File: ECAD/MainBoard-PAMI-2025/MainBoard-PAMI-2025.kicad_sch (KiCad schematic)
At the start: 52 parts, among them J1 Selecteur-Robot, J10 Serial, J11 Con_Batt, J12 BAU, J13 OLED, J2 USB_B, J3 Tirette, J4 Servo, J5 Sensor_Right, J6 Sensor_Left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

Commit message: update PCB
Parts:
- removed J12: BAU, Connector_Molex:Molex_KK-396_A-41791-0002_1x02_P3.96mm_Vertical, symbol Connector_Generic:Conn_01x02
- removed J3: Tirette, Connector_Molex:Molex_KK-254_AE-6410-02A_1x02_P2.54mm_Vertical, symbol Connector_Generic:Conn_01x02
- removed J9: Conn_01x08, symbol Connector_Generic:Conn_01x08
- removed U4, U5: TMC2208_SILENTSTEPSTICK, TMC2208_SILENTSTEPSTICK:MODULE_TMC2208_SILENTSTEPSTICK, symbol TMC2208_SILENTSTEPSTICK:TMC2208_SILENTSTEPSTICK
- added H4: MountingHole, MountingHole:MountingHole_3.2mm_M3, symbol Mechanical:MountingHole
- added SW2: SW_Reed, symbol Switch:SW_Reed
- added SW3: SW_SPDT, footprints:SK-12D10 1P2T, symbol Switch:SW_SPDT
- added U3, U4: TMC2208_SILENTSTEPSTICK, PAMI-2025:Step-Stick Driver Bottom Entry Version, symbol PAMI-2025:TMC2208_SILENTSTEPSTICK
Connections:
- net +3.3V: now also U3.10 (VIO), U4.10 (VIO)
- net +5VP: now also SW3.3 (C), U3.16 (VM), U4.16 (VM)
- net +BATT: now also SW3.2 (B)
- net EnDriver: now also U3.1 (EN), U4.1 (EN)
- net GND: now also SW2.1, U3.15 (GND), U3.9 (GND), U4.15 (GND), U4.9 (GND)
- net LeftDir: now also U4.8 (DIR)
- net LeftMS1: now also U3.2 (MS1), U4.2 (MS1)
- net LeftMS2: now also U3.3 (MS2), U4.3 (MS2)
- net LeftStep: now also U4.7 (STEP)
- net RightDir: now also U3.8 (DIR)
- net RightStep: now also U3.7 (STEP)
- net Tirette: now also SW2.2
- net at J7.1 (Pin_1): now also U4.14 (OA2)
- net at J7.2 (Pin_2): now also U4.13 (OA1)
- net at J7.3 (Pin_3): now also U4.12 (OB1)
- net at J7.4 (Pin_4): now also U4.11 (OB2)
- net at J8.1 (Pin_1): now also U3.14 (OA2)
- net at J8.2 (Pin_2): now also U3.13 (OA1)
- net at J8.3 (Pin_3): now also U3.12 (OB1)
- net at J8.4 (Pin_4): now also U3.11 (OB2)
- no-connect marks 22 -> 19
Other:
- moved on the sheet: H1, H2, H3

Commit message: Everything that need to be here :)
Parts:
- removed J5: Sensor_Right, Connector_IDC:IDC-Header_2x03_P2.54mm_Vertical, symbol Connector_Generic:Conn_02x03_Odd_Even
- removed J6: Sensor_Left, Connector_IDC:IDC-Header_2x03_P2.54mm_Vertical, symbol Connector_Generic:Conn_02x03_Odd_Even
- added J3: Sensor_RIGHT, Connector_PinSocket_2.54mm:PinSocket_1x06_P2.54mm_Vertical, symbol Connector_Generic:Conn_01x06
- added J5: Sensor_LEFT, Connector_PinSocket_2.54mm:PinSocket_1x06_P2.54mm_Vertical, symbol Connector_Generic:Conn_01x06
- added J6: Servo, Connector_PinHeader_2.54mm:PinHeader_1x03_P2.54mm_Vertical, symbol Connector_Generic:Conn_01x03
- added R12: 330R, Resistor_SMD:R_1206_3216Metric_Pad1.30x1.75mm_HandSolder, symbol Device:R_Small
- J11: footprint Connector_AMASS:AMASS_XT30U-F_1x02_P5.0mm_Vertical -> PAMI-2025:LP-e6 Batterie
- J13: footprint Connector_Molex:Molex_KK-254_AE-6410-04A_1x04_P2.54mm_Vertical -> Connector_PinSocket_2.54mm:PinSocket_1x04_P2.54mm_Vertical
- SW2: footprint (none) -> Button_Switch_SMD:SW_SPST_REED_CT05-XXXX-G1
- SW3: footprint footprints:SK-12D10 1P2T -> PAMI-2025:UB16SKW03N-C
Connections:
- net +3.3V: now also J3.1 (Pin_1), J5.1 (Pin_1)
- net +5VP: now also SW3.2 (C), J6.2 (Pin_2); no longer SW3.3 (C)
- net +BATT: now also SW3.1 (B); no longer SW3.2 (B)
- net BotNum01: now also J1.3 (Pin_3); no longer J1.4 (Pin_4)
- net BotNum02: now also J1.4 (Pin_4); no longer J1.3 (Pin_3)
- net GND: now also J3.2 (Pin_2), J5.2 (Pin_2), J6.3 (Pin_3)
- net GPIOI_LEFT: now also J5.5 (Pin_5)
- net GPIOI_RIGHT: now also J3.5 (Pin_5)
- net SCL: now also J3.3 (Pin_3), J5.3 (Pin_3)
- net SDA: now also J3.4 (Pin_4), J5.4 (Pin_4)
- net XSHUT_LEFT: now also J5.6 (Pin_6)
- net XSHUT_RIGHT: now also J3.6 (Pin_6)
- net Servo02: now reaches U1.4 (GPIO4/TOUCH4/ADC1_CH3)
- net Servo02: now also R12.1
- net Servo renamed Servo01
- new net: J6.1 (Pin_1), R12.2
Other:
- moved on the sheet: J4, R6

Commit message: Quick routing
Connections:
- net +3.3V: now also C10.2, D1.1 (VDD)
- net +5VP: no longer C10.2, D1.1 (VDD)
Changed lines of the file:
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@@
 	)
 	(symbol
+		(lib_id "power:+3.3V")
+		(at 41.91 46.99 0)
+		(unit 1)
+		(exclude_from_sim no)
+		(in_bom yes)
+		(on_board yes)
+		(dnp no)
+		(fields_autoplaced yes)
+		(property "Reference" "#PWR019"
+			(at 41.91 50.8 0)
+			(effects
+				(font
+					(size 1.27 1.27)
+				)
+				(hide yes)
+			)
+		)
+		(property "Value" "+3.3V"
+			(at 41.91 41.91 0)
+			(effects
+				(font
+					(size 1.27 1.27)
+				)
+			)
+		)
+		(property "Footprint" ""
+			(at 41.91 46.99 0)
+			(effects
+				(font
+					(size 1.27 1.27)
+				)
+				(hide yes)
+			)
+		)
+		(property "Datasheet" ""
+			(at 41.91 46.99 0)
+			(effects
+				(font
+					(size 1.27 1.27)
+				)
+				(hide yes)
+			)
+		)
+		(property "Description" ""
+			(at 41.91 46.99 0)
+			(effects
+				(font
+					(size 1.27 1.27)
+				)
+				(hide yes)
+			)
+		)
+		(pin "1"
+		)
+		(instances
+			(project "MainBoard-PAMI-2025"
+				(path "/d3e1aeb6-1412-4438-ac7d-372534bf2609"
+					(reference "#PWR019")
+					(unit 1)
+				)
+			)
+		)
+	)
+	(symbol
 		(lib_id "power:+5VP")
 		(at 54.61 27.94 0)
@@
 					(unit 1)
 				)
-			)
-		)
-	)
-	(symbol
-		(lib_id "power:+5VP")
-		(at 41.91 46.99 0)
-		(unit 1)
-		(exclude_from_sim no)
-		(in_bom yes)
-		(on_board yes)
-		(dnp no)
-		(fields_autoplaced yes)
-		(property "Reference" "#PWR019"
-			(at 41.91 50.8 0)
-			(effects
-				(font
-					(size 1.27 1.27)
-				)
-				(hide yes)
-			)
-		)
-		(property "Value" "+5VP"
-			(at 41.91 41.91 0)
-			(effects
-				(font
-					(size 1.27 1.27)
-				)
-			)
-		)
-		(property "Footprint" ""
-			(at 41.91 46.99 0)
-			(effects
-				(font
-					(size 1.27 1.27)
-				)
-				(hide yes)
-			)
-		)
-		(property "Datasheet" ""
-			(at 41.91 46.99 0)
-			(effects
-				(font
-					(size 1.27 1.27)
-				)
-				(hide yes)
-			)
-		)
-		(property "Description" ""
-			(at 41.91 46.99 0)
-			(effects
-				(font
-					(size 1.27 1.27)
-				)
-				(hide yes)
-			)
-		)
-		(pin "1"
-		)
-		(instances
-			(project "MainBoard-PAMI-2025"
-				(path "/d3e1aeb6-1412-4438-ac7d-372534bf2609"
-					(reference "#PWR019")
-					(unit 1)
-				)
-			)
-			(project "LidarBoard-2023"
-				(path "/e63e39d7-6ac0-4ffd-8aa3-1841a4541b55"
-					(reference "#PWR0125")
-					(unit 1)
-				)

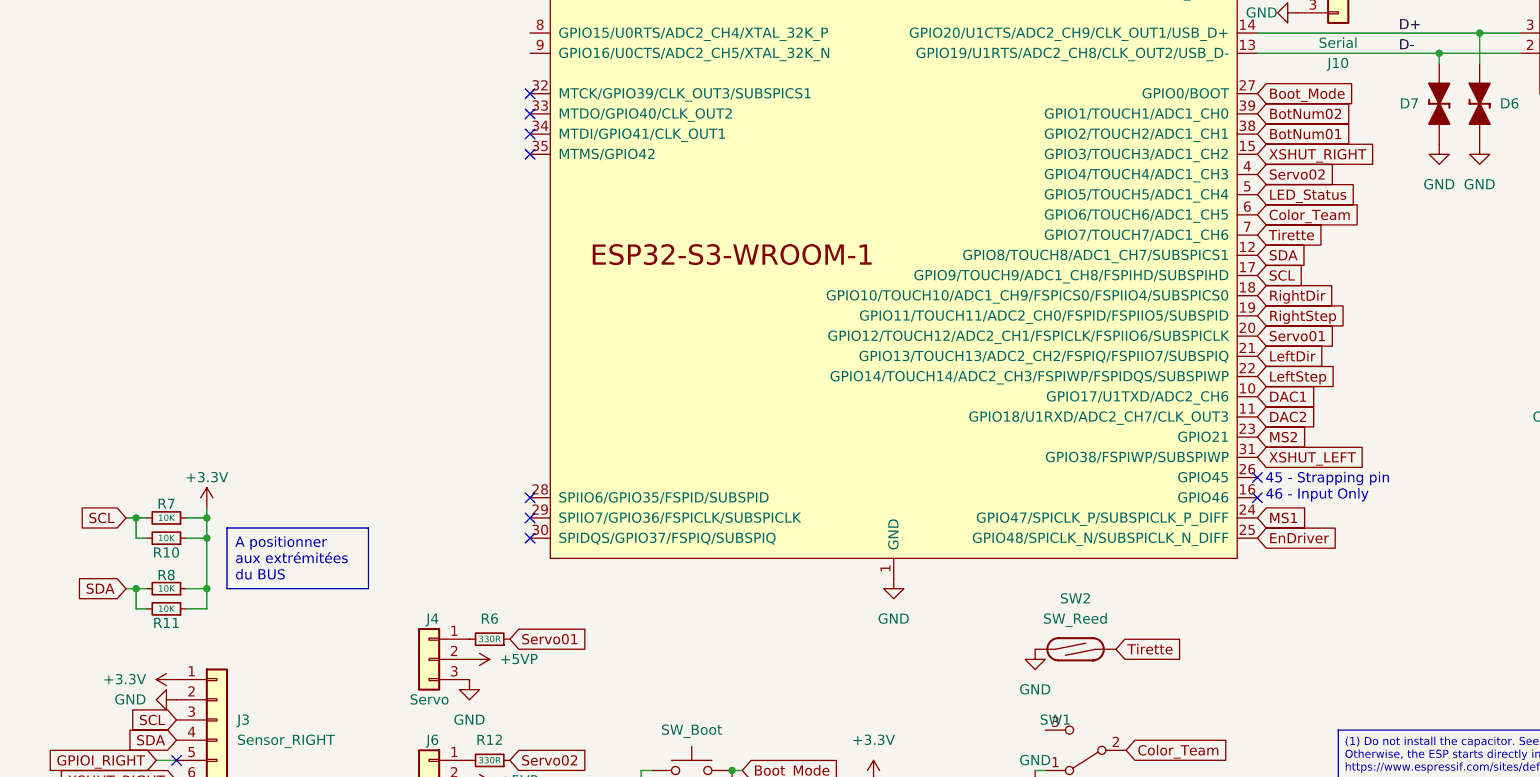
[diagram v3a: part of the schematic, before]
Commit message: Optimize routing
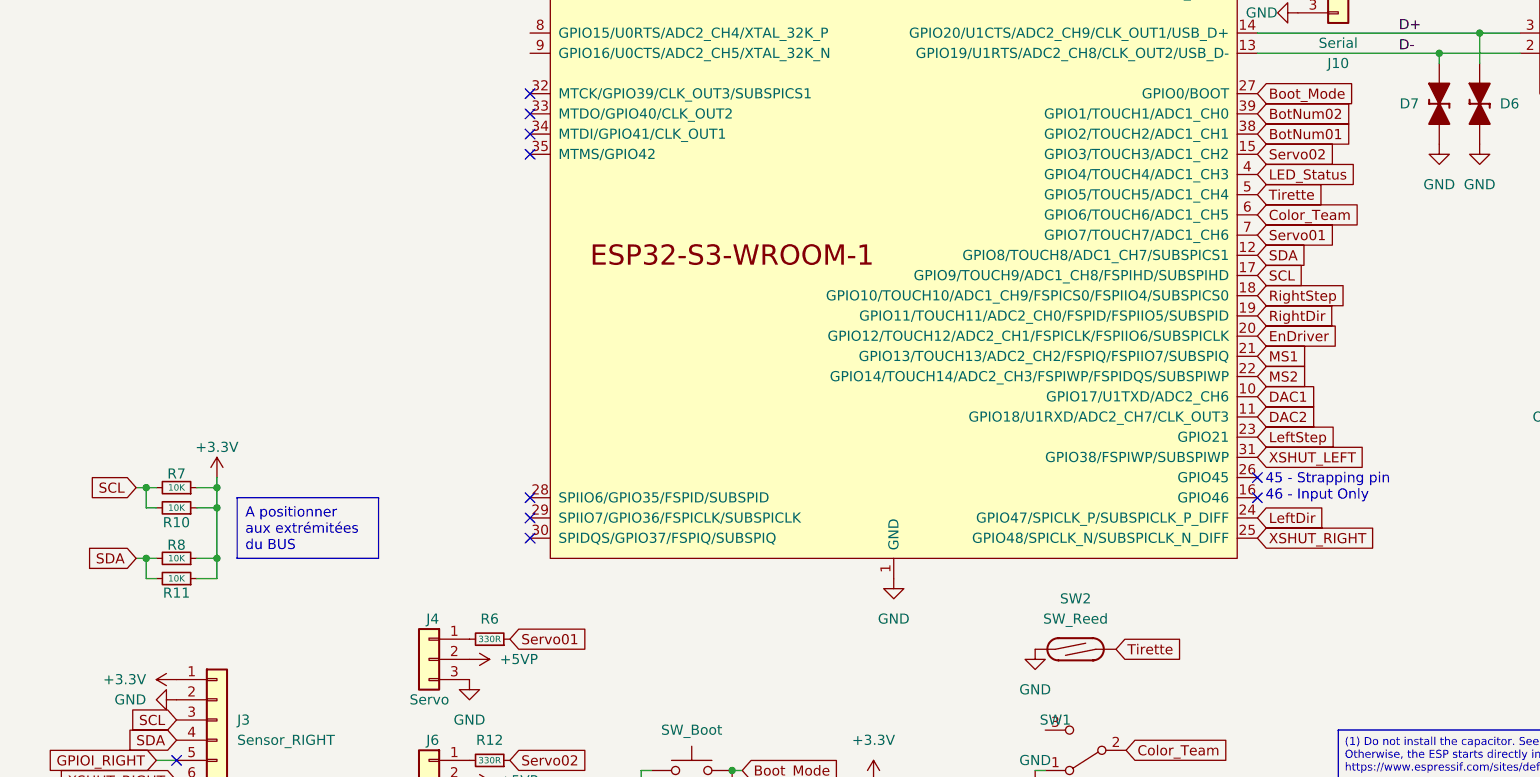
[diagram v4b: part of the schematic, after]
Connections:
- net EnDriver: now also U1.20 (GPIO12/TOUCH12/ADC2_CH1/FSPICLK/FSPIIO6/SUBSPICLK); no longer U1.25 (GPIO48/SPICLK_N/SUBSPICLK_N_DIFF)
- net LED_Status: now also U1.4 (GPIO4/TOUCH4/ADC1_CH3); no longer U1.5 (GPIO5/TOUCH5/ADC1_CH4)
- net LeftDir: now also U1.24 (GPIO47/SPICLK_P/SUBSPICLK_P_DIFF); no longer U1.21 (GPIO13/TOUCH13/ADC2_CH2/FSPIQ/FSPIIO7/SUBSPIQ)
- net LeftMS1: now also U1.21 (GPIO13/TOUCH13/ADC2_CH2/FSPIQ/FSPIIO7/SUBSPIQ); no longer U1.24 (GPIO47/SPICLK_P/SUBSPICLK_P_DIFF)
- net LeftMS2: now also U1.22 (GPIO14/TOUCH14/ADC2_CH3/FSPIWP/FSPIDQS/SUBSPIWP); no longer U1.23 (GPIO21)
- net LeftStep: now also U1.23 (GPIO21); no longer U1.22 (GPIO14/TOUCH14/ADC2_CH3/FSPIWP/FSPIDQS/SUBSPIWP)
- net RightDir: now also U1.19 (GPIO11/TOUCH11/ADC2_CH0/FSPID/FSPIIO5/SUBSPID); no longer U1.18 (GPIO10/TOUCH10/ADC1_CH9/FSPICS0/FSPIIO4/SUBSPICS0)
- net RightStep: now also U1.18 (GPIO10/TOUCH10/ADC1_CH9/FSPICS0/FSPIIO4/SUBSPICS0); no longer U1.19 (GPIO11/TOUCH11/ADC2_CH0/FSPID/FSPIIO5/SUBSPID)
- net Servo01: now also U1.7 (GPIO7/TOUCH7/ADC1_CH6); no longer U1.20 (GPIO12/TOUCH12/ADC2_CH1/FSPICLK/FSPIIO6/SUBSPICLK)
- net Servo02: now also U1.15 (GPIO3/TOUCH3/ADC1_CH2); no longer U1.4 (GPIO4/TOUCH4/ADC1_CH3)
- net Tirette: now also U1.5 (GPIO5/TOUCH5/ADC1_CH4); no longer U1.7 (GPIO7/TOUCH7/ADC1_CH6)
- net XSHUT_RIGHT: now also U1.25 (GPIO48/SPICLK_N/SUBSPICLK_N_DIFF); no longer U1.15 (GPIO3/TOUCH3/ADC1_CH2)
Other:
- moved on the sheet: R10, R11, R7, R8

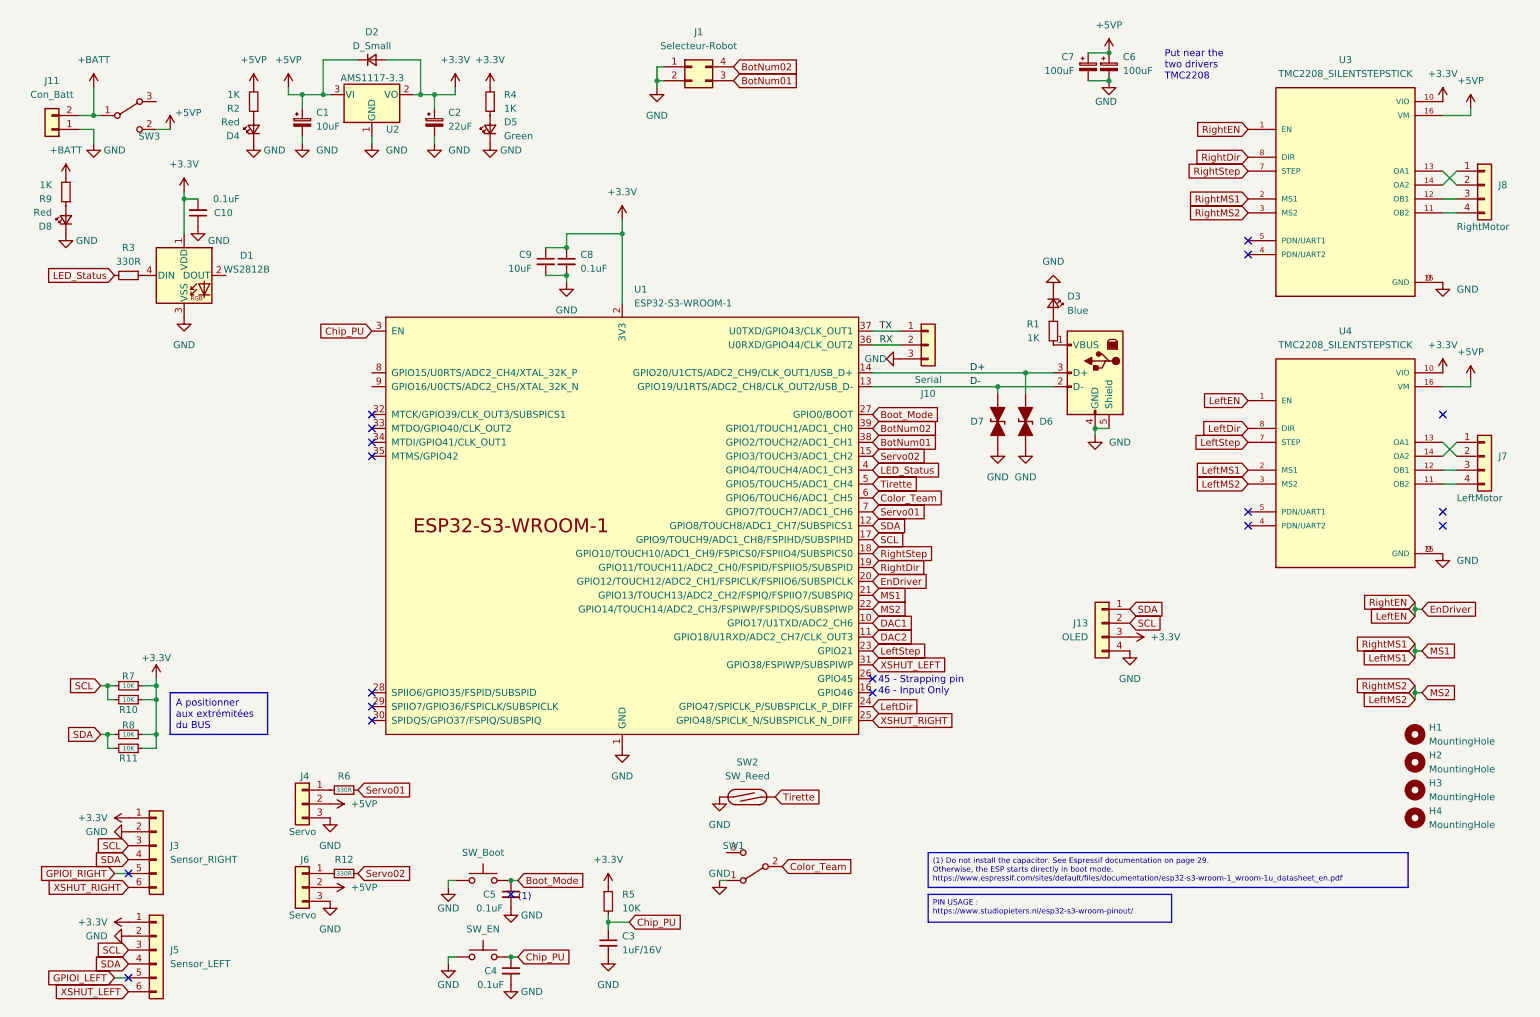
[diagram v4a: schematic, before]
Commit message: Change switch + regulator + Servo Power
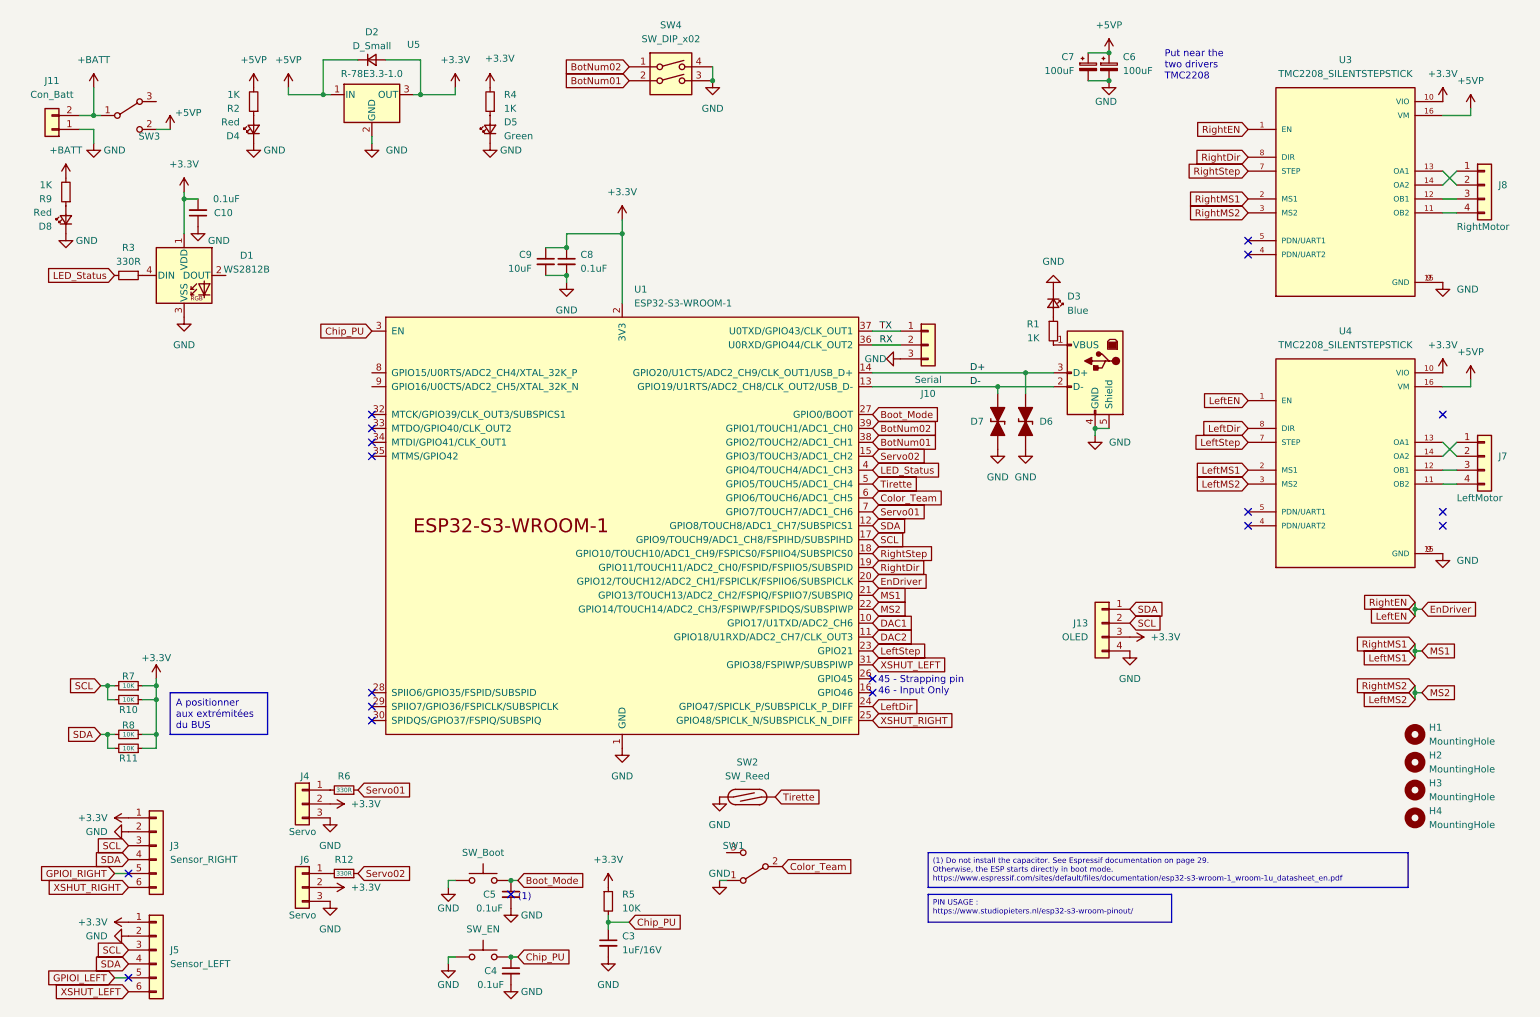
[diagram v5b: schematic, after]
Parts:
- removed C1: 10uF, Capacitor_SMD:CP_Elec_5x5.4, symbol Device:C_Polarized_Small
- removed C2: 22uF, Capacitor_Tantalum_SMD:CP_EIA-3528-12_Kemet-T_Pad1.50x2.35mm_HandSolder, symbol Device:C_Polarized_Small
- removed J1: Selecteur-Robot, Connector_PinHeader_2.54mm:PinHeader_2x02_P2.54mm_Vertical, symbol Connector_Generic:Conn_02x02_Counter_Clockwise
- removed U2: AMS1117-3.3, Package_TO_SOT_SMD:SOT-223-3_TabPin2, symbol Regulator_Linear:AMS1117-3.3
- added SW4: SW_DIP_x02, Button_Switch_THT:SW_DIP_SPSTx02_Slide_9.78x7.26mm_W7.62mm_P2.54mm, symbol Switch:SW_DIP_x02
- added U5: R-78E3.3-1.0, Converter_DCDC:Converter_DCDC_RECOM_R-78E-0.5_THT, symbol Regulator_Switching:R-78E3.3-1.0
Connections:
- net +3.3V: now also J4.2 (Pin_2), J6.2 (Pin_2), U5.3 (OUT)
- net +5VP: now also U5.1 (IN); no longer J4.2 (Pin_2), J6.2 (Pin_2)
- net BotNum01: now also SW4.2
- net BotNum02: now also SW4.1
- net GND: now also SW4.3, SW4.4, U5.2 (GND)

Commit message: add sensor center
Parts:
- added J1: Sensor_Center, Connector_PinSocket_2.54mm:PinSocket_1x06_P2.54mm_Vertical, symbol Connector_Generic:Conn_01x06
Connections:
- net +3.3V: now also J1.1 (Pin_1)
- net GND: now also J1.2 (Pin_2)
- net SCL: now also J1.3 (Pin_3)
- net SDA: now also J1.4 (Pin_4)
- new net GPIOI_CENTER: J1.5 (Pin_5)
- new net XSHUT_CENTER: J1.6 (Pin_6)
- no-connect marks 19 -> 20
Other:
- moved on the sheet: J3, R10, R11, R7, R8
